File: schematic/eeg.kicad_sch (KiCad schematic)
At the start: 25 parts, among them IC1 INA121PA, U1 LF353P, U2 LF353P

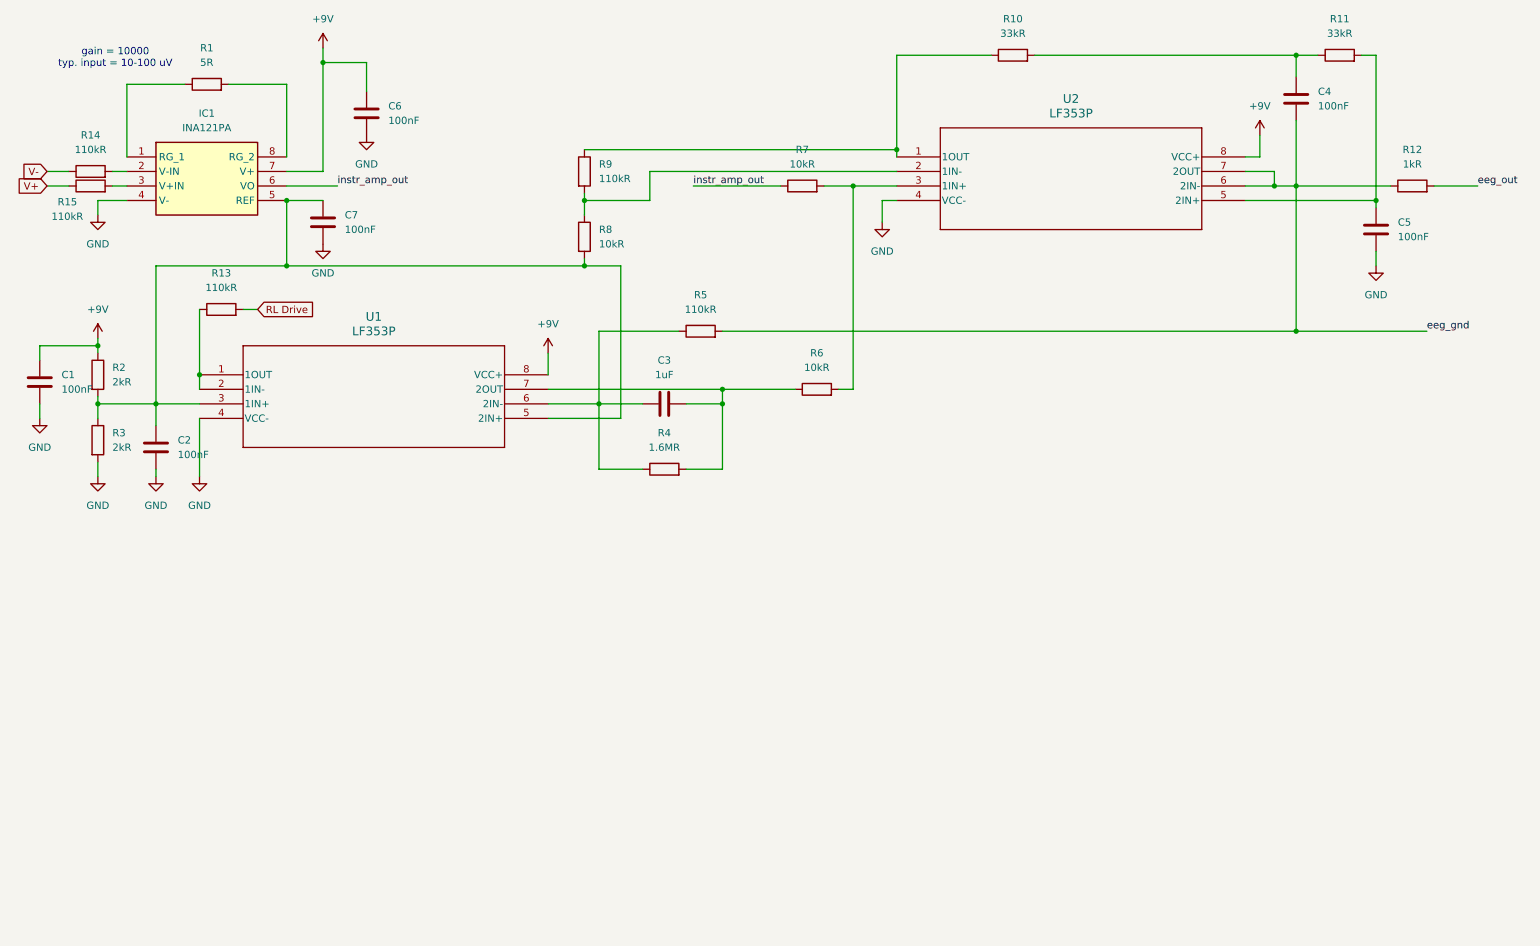
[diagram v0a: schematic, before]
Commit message: updated schematic to be correct based on simulation
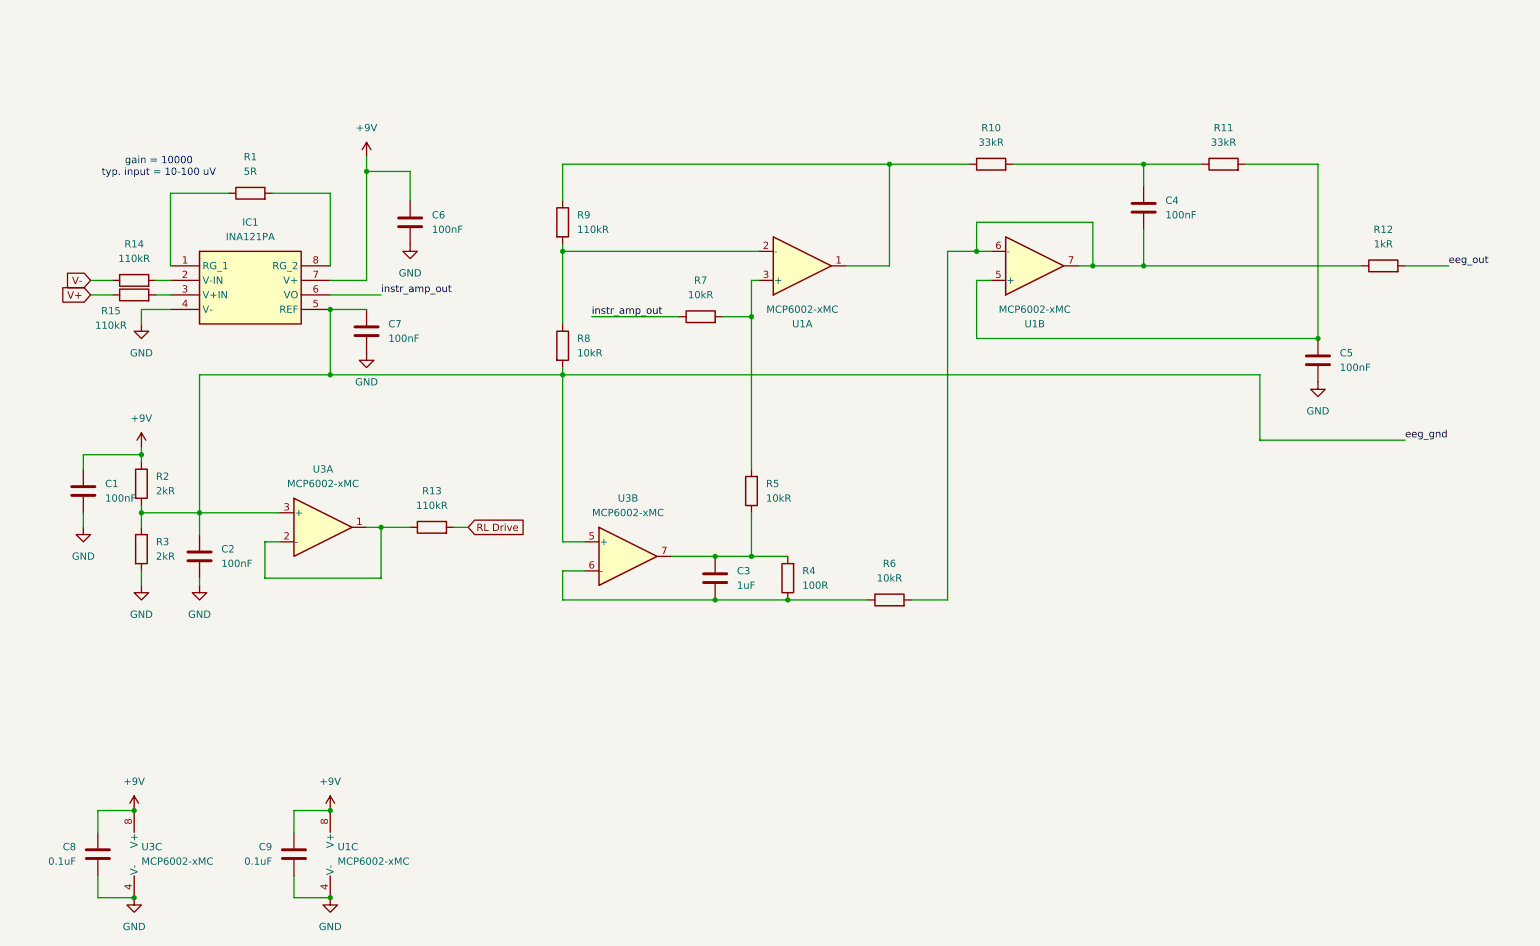
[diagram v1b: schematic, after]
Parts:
- removed U1, U2: LF353P, P8, symbol 2025-10-29_20-49-19:LF353P
- added C8, C9: 0.1uF, symbol Device:C
- added U1, U3: MCP6002-xMC, Package_DFN_QFN:DFN-8-1EP_3x2mm_P0.5mm_EP1.75x1.45mm, symbol Amplifier_Operational:MCP6002-xMC
- R4: value 1.6MR -> 100R
- R5: value 110kR -> 10kR
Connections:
- net +9V: now also C8.2, C9.1, U1.8 (V+), U3.8 (V+)
- net GND: now also C8.1, C9.2, U1.4 (V-), U1.9 (V-), U3.4 (V-), U3.9 (V-)
- net eeg_gnd: now also C2.1, C7.1, IC1.5 (REF), R2.2, R3.1, R8.2, U3.3 (+), U3.5 (+); no longer C4.2, R12.1, R5.2
- net at R6.2: now also C4.2, R12.1, U1.6 (-), U1.7; no longer R7.2
- net at R13.1: now also U3.1, U3.2 (-)
- net at C3.1, R4.1: now also R6.1, U3.6 (-); no longer R5.1
- net at C3.2, R4.2: now also R5.1, U3.7; no longer R6.1
- net at R10.1, R9.1: now also U1.1
- net at R8.1, R9.2: now also U1.2 (-)
- net at C5.1, R11.2: now also U1.5 (+)
- new net: R5.2, R7.2, U1.3 (+)
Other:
- moved on the sheet: C1, C2, C3, C4, C5, C6, C7, IC1, R1, R10, R11, R12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
